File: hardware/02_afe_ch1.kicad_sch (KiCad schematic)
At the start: 0 parts

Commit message: AFE ch1: compensated divider with offset injection
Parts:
- added C5, C6: 5-60pF, symbol Device:C_Variable
- added J2: BNC_CH1, symbol Connector:Conn_Coaxial
- added R4: 750K, symbol Device:R
- added R5: 250K, symbol Device:R
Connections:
- new net: C5.1, J2.1 (In), R4.1
- new net: C5.2, C6.1, R4.2, R5.1
- new net GND: J2.2 (Ext)
- new net VREF_2V2: C6.2, R5.2
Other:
- note added: "Compensation: adjust C5 so R4*C5 = R5*C6. Tune with 1kHz square wave: flat top = correct, sagging = undercomp, overshoot = overcomp."
- note added: "R3/R4 values are NOMINAL. Measure the actual pair on the DMM and store the measured ratio as a calibration constant in firmware (oscil_cal.h). Ratio sets gain; sum sets input Z. Absolute value does not matter, matching does."
- note added: "Single-ended, NOT isolated. Shell = system GND = USB GND = mains earth. Max +/-5V direct, +/-50V with 10x probe. NEVER connect to mains."

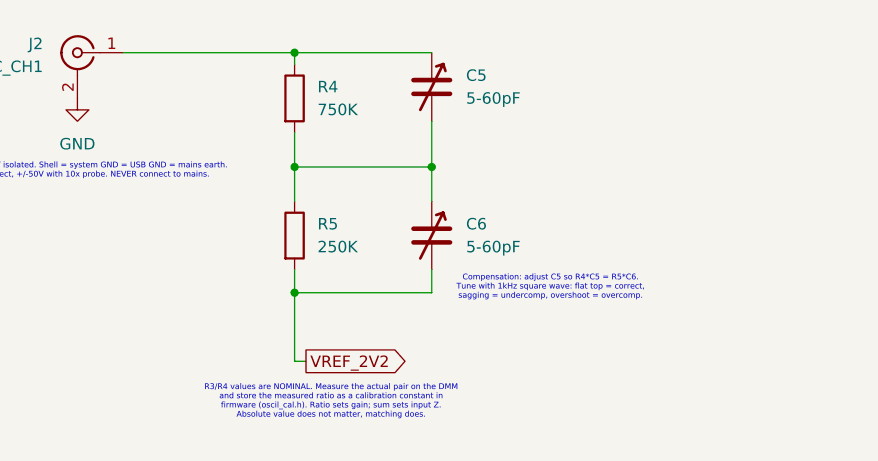
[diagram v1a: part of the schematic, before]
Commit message: AFE ch1: input clamp
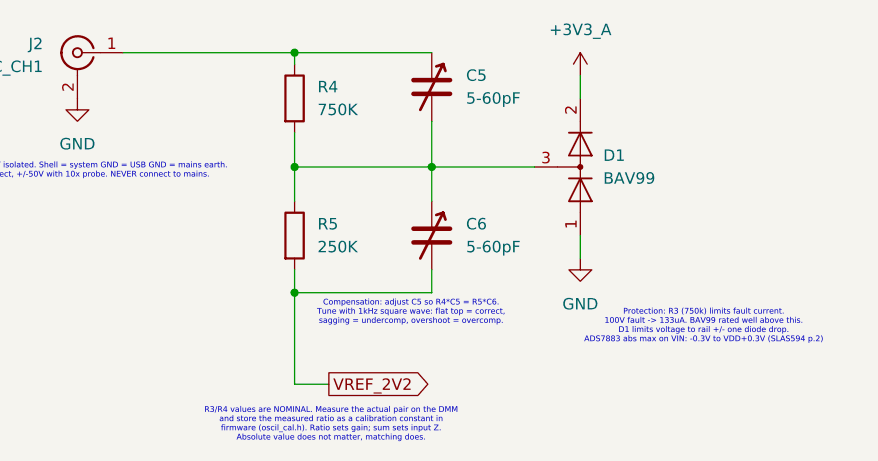
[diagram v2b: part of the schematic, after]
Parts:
- added D1: BAV99, Package_TO_SOT_SMD:SOT-23, symbol Diode:BAV99
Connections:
- net GND: now also D1.1 (K)
- net at C5.2, C6.1, R4.2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: now also D1.3 (K)
- new net +3V3_A: D1.2 (A)
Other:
- note added: "Protection: R3 (750k) limits fault current. 100V fault -> 133uA. BAV99 rated well above this. D1 limits voltage to rail +/- one diode drop. ADS7883 abs max on VIN: -0.3V to VDD+0.3V (SLAS594 p.2)"

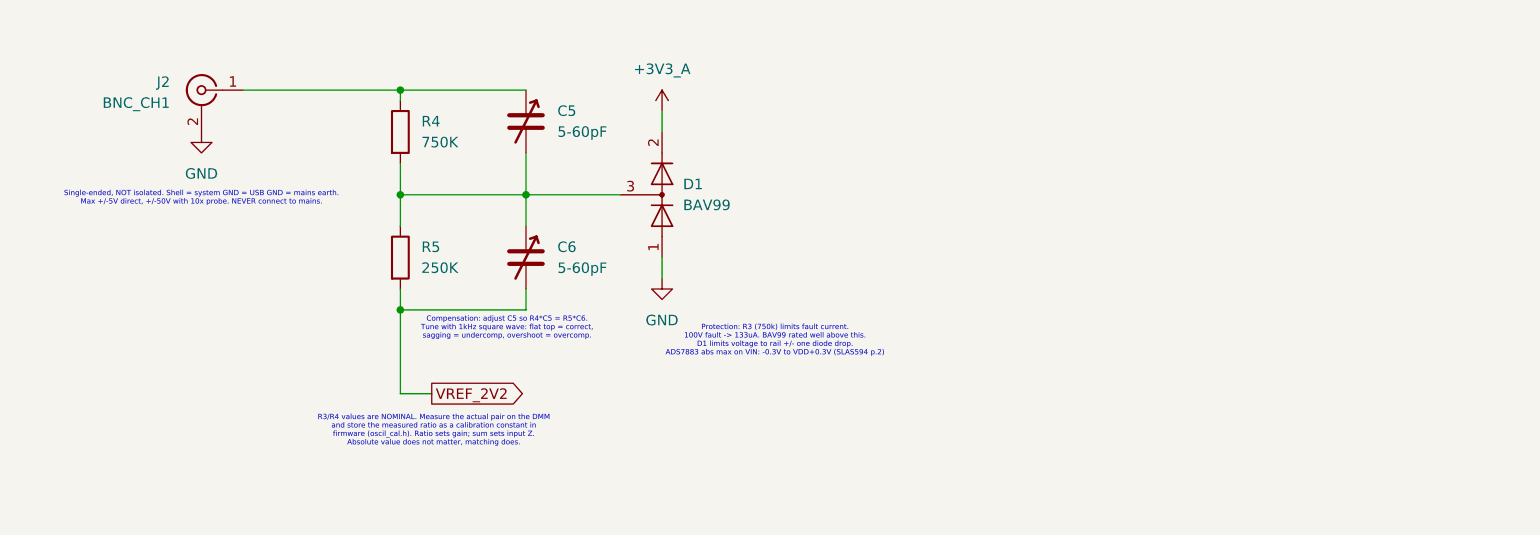
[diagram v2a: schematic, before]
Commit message: AFE ch1: unity-gain buffer
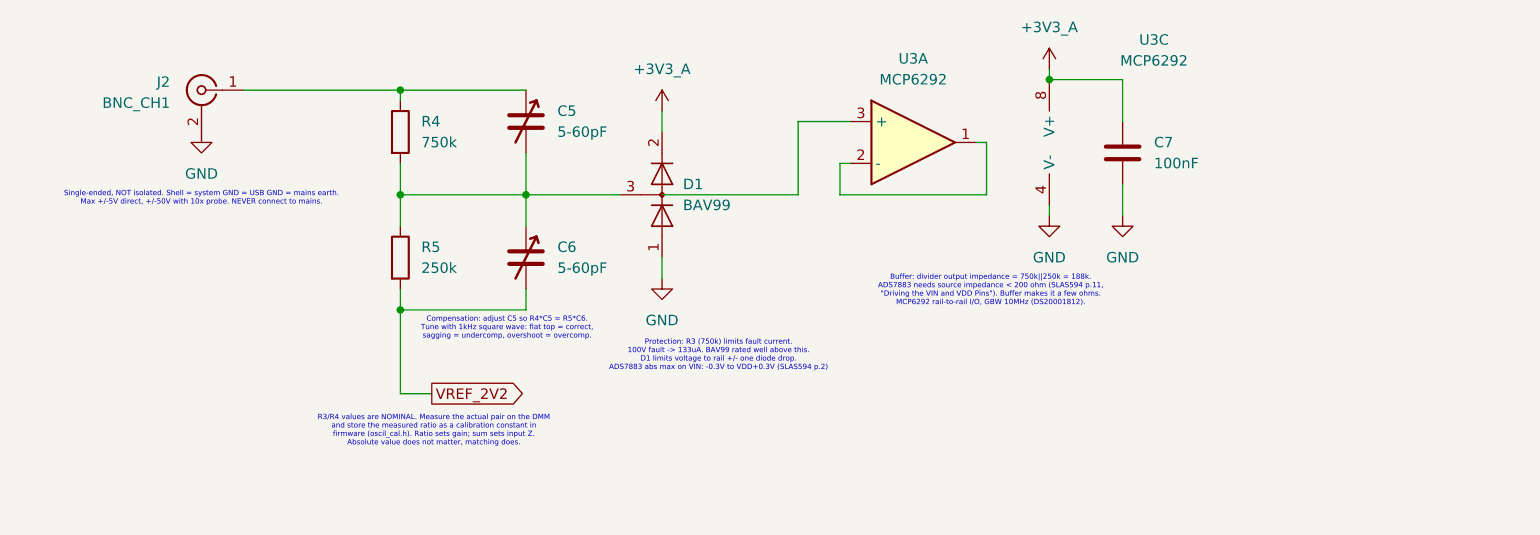
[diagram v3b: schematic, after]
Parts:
- added C7: 100nF, Package_SO:SOIC-8_3.9x4.9mm_P1.27mm, symbol Device:C
- added U3: MCP6292, Package_TO_SOT_SMD:SOT-353_SC-70-5, symbol Amplifier_Operational:Opamp_Dual
- R4: value 750K -> 750k
- R5: value 250K -> 250k
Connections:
- net +3V3_A: now also C7.1, U3.8 (V+)
- net GND: now also C7.2, U3.4 (V-)
- new net: U3.1, U3.2 (-)
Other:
- note added: "Buffer: divider output impedance = 750k||250k = 188k. ADS7883 needs source impedance < 200 ohm (SLAS594 p.11, "Driving the VIN and VDD Pins"). Buffer makes it a few ohms. MCP6292 rail-to-rail I/O, GBW 10MHz (DS20001812)."

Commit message: AFE channel 1: divider, compensation, clamp, buffer, filter
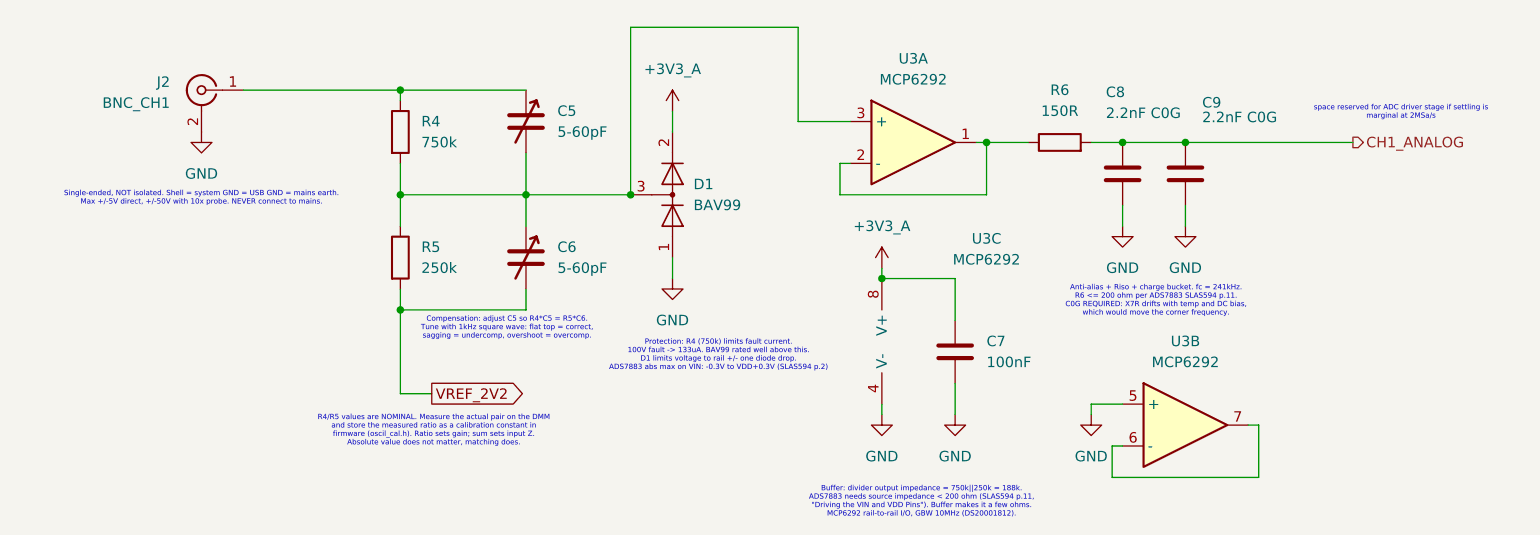
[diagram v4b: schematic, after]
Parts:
- added C8, C9: 2.2nF C0G, Package_SO:SOIC-8_3.9x4.9mm_P1.27mm, symbol Device:C
- added R6: 150R, symbol Device:R
- added unit 2 of U3
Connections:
- net GND: now also C8.2, C9.2, U3.5 (+)
- net at C5.2, C6.1, D1.3 (K)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: now also U3.3 (+)
- net at U3.1, U3.2 (-): now also R6.1
- new net: U3.6 (-), U3.7
- new net CH1_ANALOG: C8.1, C9.1, R6.2
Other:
- note added: "Anti-alias + Riso + charge bucket. fc = 241kHz. R6 <= 200 ohm per ADS7883 SLAS594 p.11. C0G REQUIRED: X7R drifts with temp and DC bias, which would move the corner frequency."
- note added: "Protection: R4 (750k) limits fault current. 100V fault -> 133uA. BAV99 rated well above this. D1 limits voltage to rail +/- one diode drop. ADS7883 abs max on VIN: -0.3V to VDD+0.3V (SLAS594 p.2)"
- note added: "R4/R5 values are NOMINAL. Measure the actual pair on the DMM and store the measured ratio as a calibration constant in firmware (oscil_cal.h). Ratio sets gain; sum sets input Z. Absolute value does not matter, matching does."
- note added: "space reserved for ADC driver stage if settling is marginal at 2MSa/s"
- note removed: "Protection: R3 (750k) limits fault current. 100V fault -> 133uA. BAV99 rated well above this. D1 limits voltage to rail +/- one diode drop. ADS7883 abs max on VIN: -0.3V to VDD+0.3V (SLAS594 p.2)"
- note removed: "R3/R4 values are NOMINAL. Measure the actual pair on the DMM and store the measured ratio as a calibration constant in firmware (oscil_cal.h). Ratio sets gain; sum sets input Z. Absolute value does not matter, matching does."
- moved on the sheet: C7, D1, U3C

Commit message: Add final Rev A schematic PDF and edited footprints
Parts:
- C5, C6: footprint (none) -> Capacitor_SMD:C_Trimmer_Murata_TZB4-A
- C7, C8, C9: footprint Package_SO:SOIC-8_3.9x4.9mm_P1.27mm -> Capacitor_THT:C_Disc_D5.0mm_W2.5mm_P5.00mm
- J2: footprint (none) -> Connector_Coaxial:BNC_PanelMountable_Vertical
- R4, R5, R6: footprint (none) -> Resistor_THT:R_Axial_DIN0207_L6.3mm_D2.5mm_P10.16mm_Horizontal
- U3: footprint Package_TO_SOT_SMD:SOT-353_SC-70-5 -> Package_DIP:DIP-8_W7.62mm
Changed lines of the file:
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@@
 	(title_block
 		(title "Oscil")
-		(date "2026-09-18")
-		(rev "0.1")
+		(date "2026-09-21")
+		(rev "A")
 		(comment 1 "Two-channel Digital Oscilloscope and Function Generator")
 		(comment 2 "ESP32-S3 / ESP-IDF / FreeRTOS")
@@
 			)
 		)
-		(property "Footprint" ""
+		(property "Footprint" "Connector_Coaxial:BNC_PanelMountable_Vertical"
 			(at 38.1 40.64 0)
 			(hide yes)
@@
 			)
 		)
-		(property "Footprint" ""
+		(property "Footprint" "Capacitor_SMD:C_Trimmer_Murata_TZB4-A"
 			(at 77.47 44.45 0)
 			(hide yes)
@@
 			)
 		)
-		(property "Footprint" "Package_SO:SOIC-8_3.9x4.9mm_P1.27mm"
+		(property "Footprint" "Capacitor_THT:C_Disc_D5.0mm_W2.5mm_P5.00mm"
 			(at 150.8252 54.61 0)
 			(hide yes)
@@
 			)
 		)
-		(property "Footprint" "Package_TO_SOT_SMD:SOT-353_SC-70-5"
+		(property "Footprint" "Package_DIP:DIP-8_W7.62mm"
 			(at 157.48 81.28 0)
 			(hide yes)
@@
 			)
 		)
-		(property "Footprint" "Package_TO_SOT_SMD:SOT-353_SC-70-5"
+		(property "Footprint" "Package_DIP:DIP-8_W7.62mm"
 			(at 123.19 71.12 0)
 			(hide yes)
@@
 			)
 		)
-		(property "Footprint" ""
+		(property "Footprint" "Resistor_THT:R_Axial_DIN0207_L6.3mm_D2.5mm_P10.16mm_Horizontal"
 			(at 142.24 48.768 90)
 			(hide yes)
@@
 			)
 		)
-		(property "Footprint" ""
+		(property "Footprint" "Resistor_THT:R_Axial_DIN0207_L6.3mm_D2.5mm_P10.16mm_Horizontal"
 			(at 60.452 60.96 90)
 			(hide yes)
@@
 			)
 		)
-		(property "Footprint" "Package_TO_SOT_SMD:SOT-353_SC-70-5"
+		(property "Footprint" "Package_DIP:DIP-8_W7.62mm"
 			(at 124.46 46.99 0)
 			(hide yes)
@@
 			)
 		)
-		(property "Footprint" ""
+		(property "Footprint" "Capacitor_SMD:C_Trimmer_Murata_TZB4-A"
 			(at 77.47 60.96 0)
 			(hide yes)
@@
 			)
 		)
-		(property "Footprint" "Package_SO:SOIC-8_3.9x4.9mm_P1.27mm"
+		(property "Footprint" "Capacitor_THT:C_Disc_D5.0mm_W2.5mm_P5.00mm"
 			(at 130.5052 76.2 0)
 			(hide yes)
@@
 			)
 		)
-		(property "Footprint" ""
+		(property "Footprint" "Resistor_THT:R_Axial_DIN0207_L6.3mm_D2.5mm_P10.16mm_Horizontal"
 			(at 60.452 45.72 90)
 			(hide yes)
@@
 			)
 		)
-		(property "Footprint" "Package_SO:SOIC-8_3.9x4.9mm_P1.27mm"
+		(property "Footprint" "Capacitor_THT:C_Disc_D5.0mm_W2.5mm_P5.00mm"
 			(at 158.4452 54.61 0)
 			(hide yes)
